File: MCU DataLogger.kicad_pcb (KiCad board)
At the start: 2 copper layers, 51 x 35 mm, 29 parts, among them J1 Conn_01x04_Pin, J2 Conn_01x09_Pin, J3 Conn_01x04_Pin, J4 Conn_02x03_Odd_Even, U1 24LC1025, U2 DS1337S_, U3 24LC1025, U4 ATMEGA328P-AU, Y1 32.768 KH, Y2 16MHz

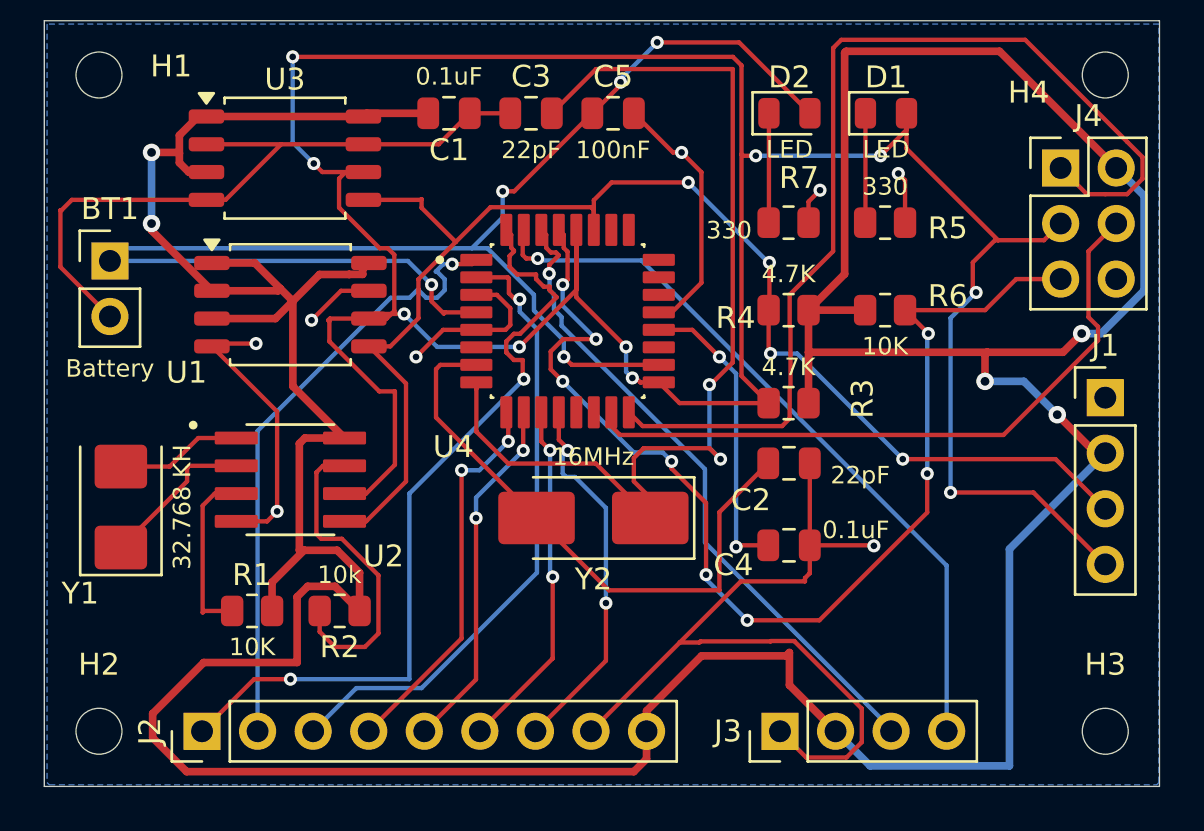
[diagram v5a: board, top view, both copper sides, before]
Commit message: Added labels and callouts to the front layer of the silk screen and reran erc check... 0 warnings one GND pad error (severity 0)
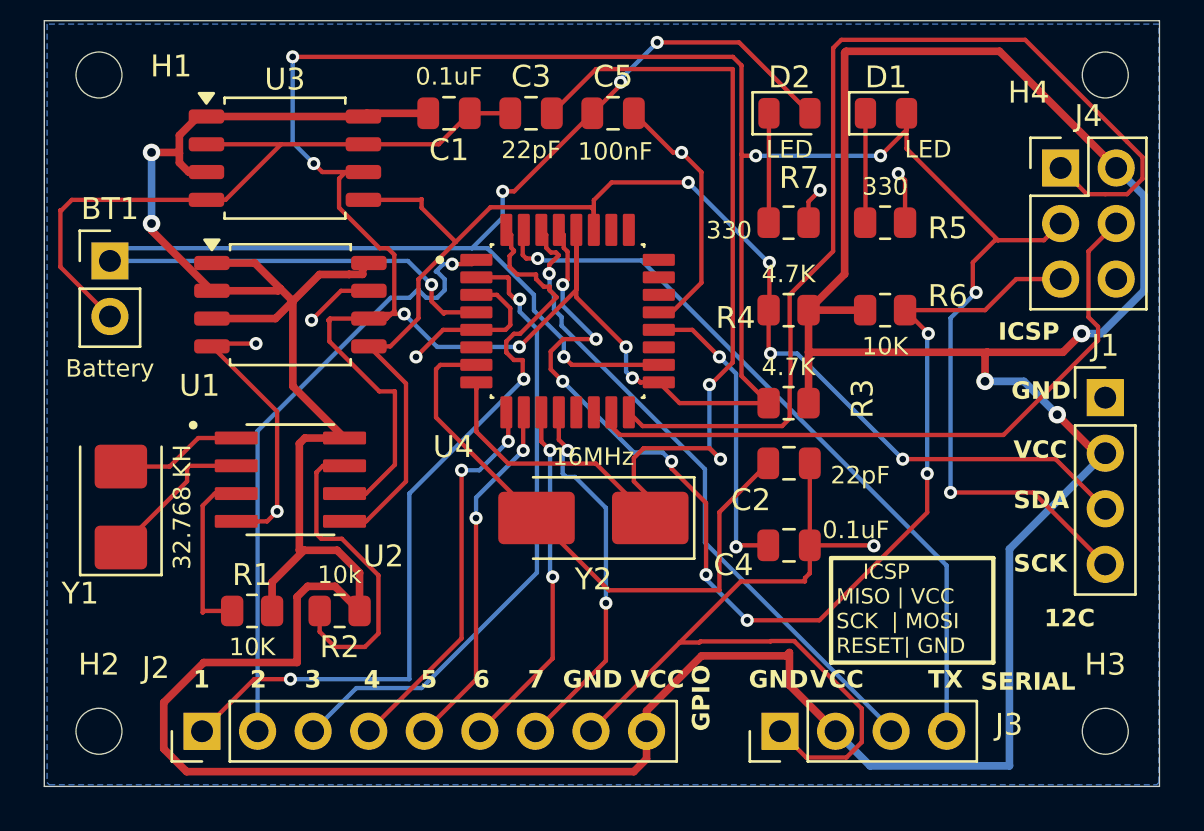
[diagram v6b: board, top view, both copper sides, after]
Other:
- board text added: "1"
- board text added: "12C"
- board text added: "2"
- board text added: "3"
- board text added: "4"
- board text added: "5"
- board text added: "6"
- board text added: "7"
- board text added: "GND"
- board text added: "GPIO"
- board text added: "ICSP"
- board text added: "ICSP MISO | VCC SCK | MOSI RESET| GND"
- board text added: "SCK"
- board text added: "SDA"
- board text added: "SERIAL"
- board text added: "TX"
- board text added: "VCC"
